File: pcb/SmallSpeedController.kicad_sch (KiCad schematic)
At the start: 38 parts, among them J1 Conn_01x02_Socket, J10 Conn_01x03_Socket, J11 Conn_01x03_Socket, J2 Conn_01x02_Socket, J4 Conn_01x02_Socket, J5 Conn_01x04_Socket, J6 Conn_01x04_Socket, J9 Conn_01x03_Socket, SW2 TS-1088-AR02016, U2 AMS1117-3.3, U3 DRV8837DSGR, U4 DRV8837DSGR, U5 CH32V003FxUx

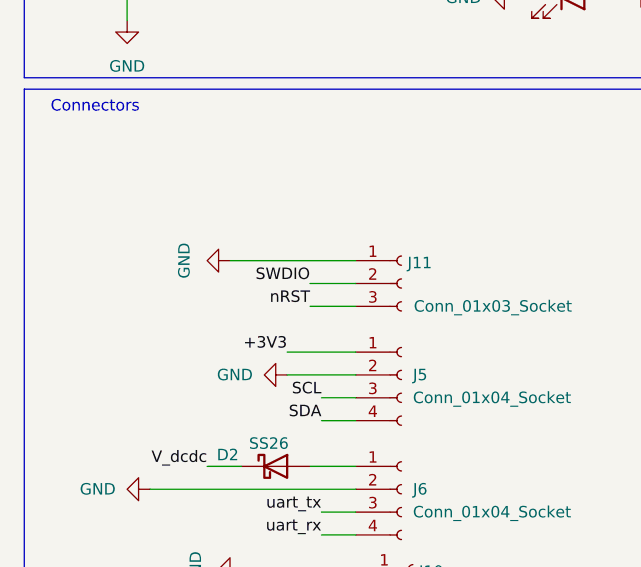
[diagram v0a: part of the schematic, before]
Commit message: pcb, sch: small cleanups for next fabrication round
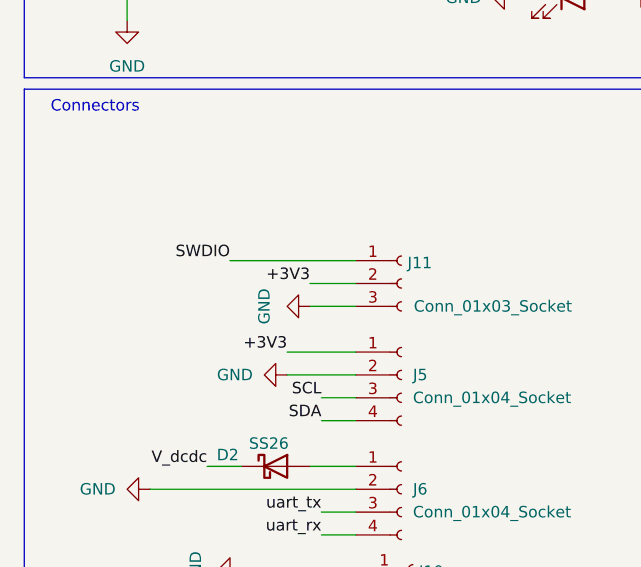
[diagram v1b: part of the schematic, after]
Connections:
- net +3V3: now also J11.2 (Pin_2)
- net GND: now also J11.3 (Pin_3); no longer J11.1 (Pin_1)
- net SWDIO: now also J11.1 (Pin_1); no longer J11.2 (Pin_2)
- net nRST: no longer J11.3 (Pin_3)
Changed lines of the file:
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@@
 		)
 	)
-	(label "SWDIO"
+	(label "+3V3"
 		(at 50.8 148.59 180)
 		(effects
@@
 		)
 	)
-	(label "nRST"
-		(at 50.8 151.13 180)
-		(effects
-			(font
-				(size 1.27 1.27)
-			)
-			(justify right bottom)
-		)
-	)
 	(label "pwm_speed_input2"
 		(at 201.93 170.18 0)
@@
 		)
 	)
+	(label "SWDIO"
+		(at 41.91 146.05 180)
+		(effects
+			(font
+				(size 1.27 1.27)
+			)
+			(justify right bottom)
+		)
+	)
 	(label "motcon1_pwm_in1"
 		(at 181.61 43.18 0)
@@
 	)
 	(symbol
+		(lib_id "power:GND")
+		(at 50.8 151.13 270)
+		(unit 1)
+		(exclude_from_sim no)
+		(in_bom yes)
+		(on_board yes)
+		(dnp no)
+		(property "Reference" "#PWR010"
+			(at 44.45 151.13 0)
+			(effects
+				(font
+					(size 1.27 1.27)
+				)
+				(hide yes)
+			)
+		)
+		(property "Value" "GND"
+			(at 45.72 151.13 0)
+			(effects
+				(font
+					(size 1.27 1.27)
+				)
+			)
+		)
+		(property "Footprint" ""
+			(at 50.8 151.13 0)
+			(effects
+				(font
+					(size 1.27 1.27)
+				)
+				(hide yes)
+			)
+		)
+		(property "Datasheet" ""
+			(at 50.8 151.13 0)
+			(effects
+				(font
+					(size 1.27 1.27)
+				)
+				(hide yes)
+			)
+		)
+		(property "Description" "Power symbol creates a global label with name \"GND\" , ground"
+			(at 50.8 151.13 0)
+			(effects
+				(font
+					(size 1.27 1.27)
+				)
+				(hide yes)
+			)
+		)
+		(pin "1"
+		)
+		(instances
+			(project "SmallSpeedController"
+				(path "/ad61fa74-e1dd-4b78-9d6b-122c1a722d03"
+					(reference "#PWR010")
+					(unit 1)
+				)
+			)
+		)
+	)
+	(symbol
 		(lib_id "Device:C")
 		(at 130.81 91.44 0)
@@
 					(unit 1)
 				)
-			)
-		)
-	)
-	(symbol
-		(lib_id "power:GND")
-		(at 41.91 146.05 270)
-		(unit 1)
-		(exclude_from_sim no)
-		(in_bom yes)
-		(on_board yes)
-		(dnp no)
-		(property "Reference" "#PWR031"
-			(at 35.56 146.05 0)
-			(effects
-				(font
-					(size 1.27 1.27)
-				)
-				(hide yes)
-			)
-		)
-		(property "Value" "GND"
-			(at 36.83 146.05 0)
-			(effects
-				(font
-					(size 1.27 1.27)
-				)
-			)
-		)
-		(property "Footprint" ""
-			(at 41.91 146.05 0)
-			(effects
-				(font
-					(size 1.27 1.27)
-				)
-				(hide yes)
-			)
-		)
-		(property "Datasheet" ""
-			(at 41.91 146.05 0)
-			(effects
-				(font
-					(size 1.27 1.27)
-				)
-				(hide yes)
-			)
-		)
-		(property "Description" "Power symbol creates a global label with name \"GND\" , ground"
-			(at 41.91 146.05 0)
-			(effects
-				(font
-					(size 1.27 1.27)
-				)
-				(hide yes)
-			)
-		)
-		(pin "1"
-		)
-		(instances
-			(project "MiniRiscVBot"
-				(path "/ad61fa74-e1dd-4b78-9d6b-122c1a722d03"
-					(reference "#PWR031")
-					(unit 1)
-				)

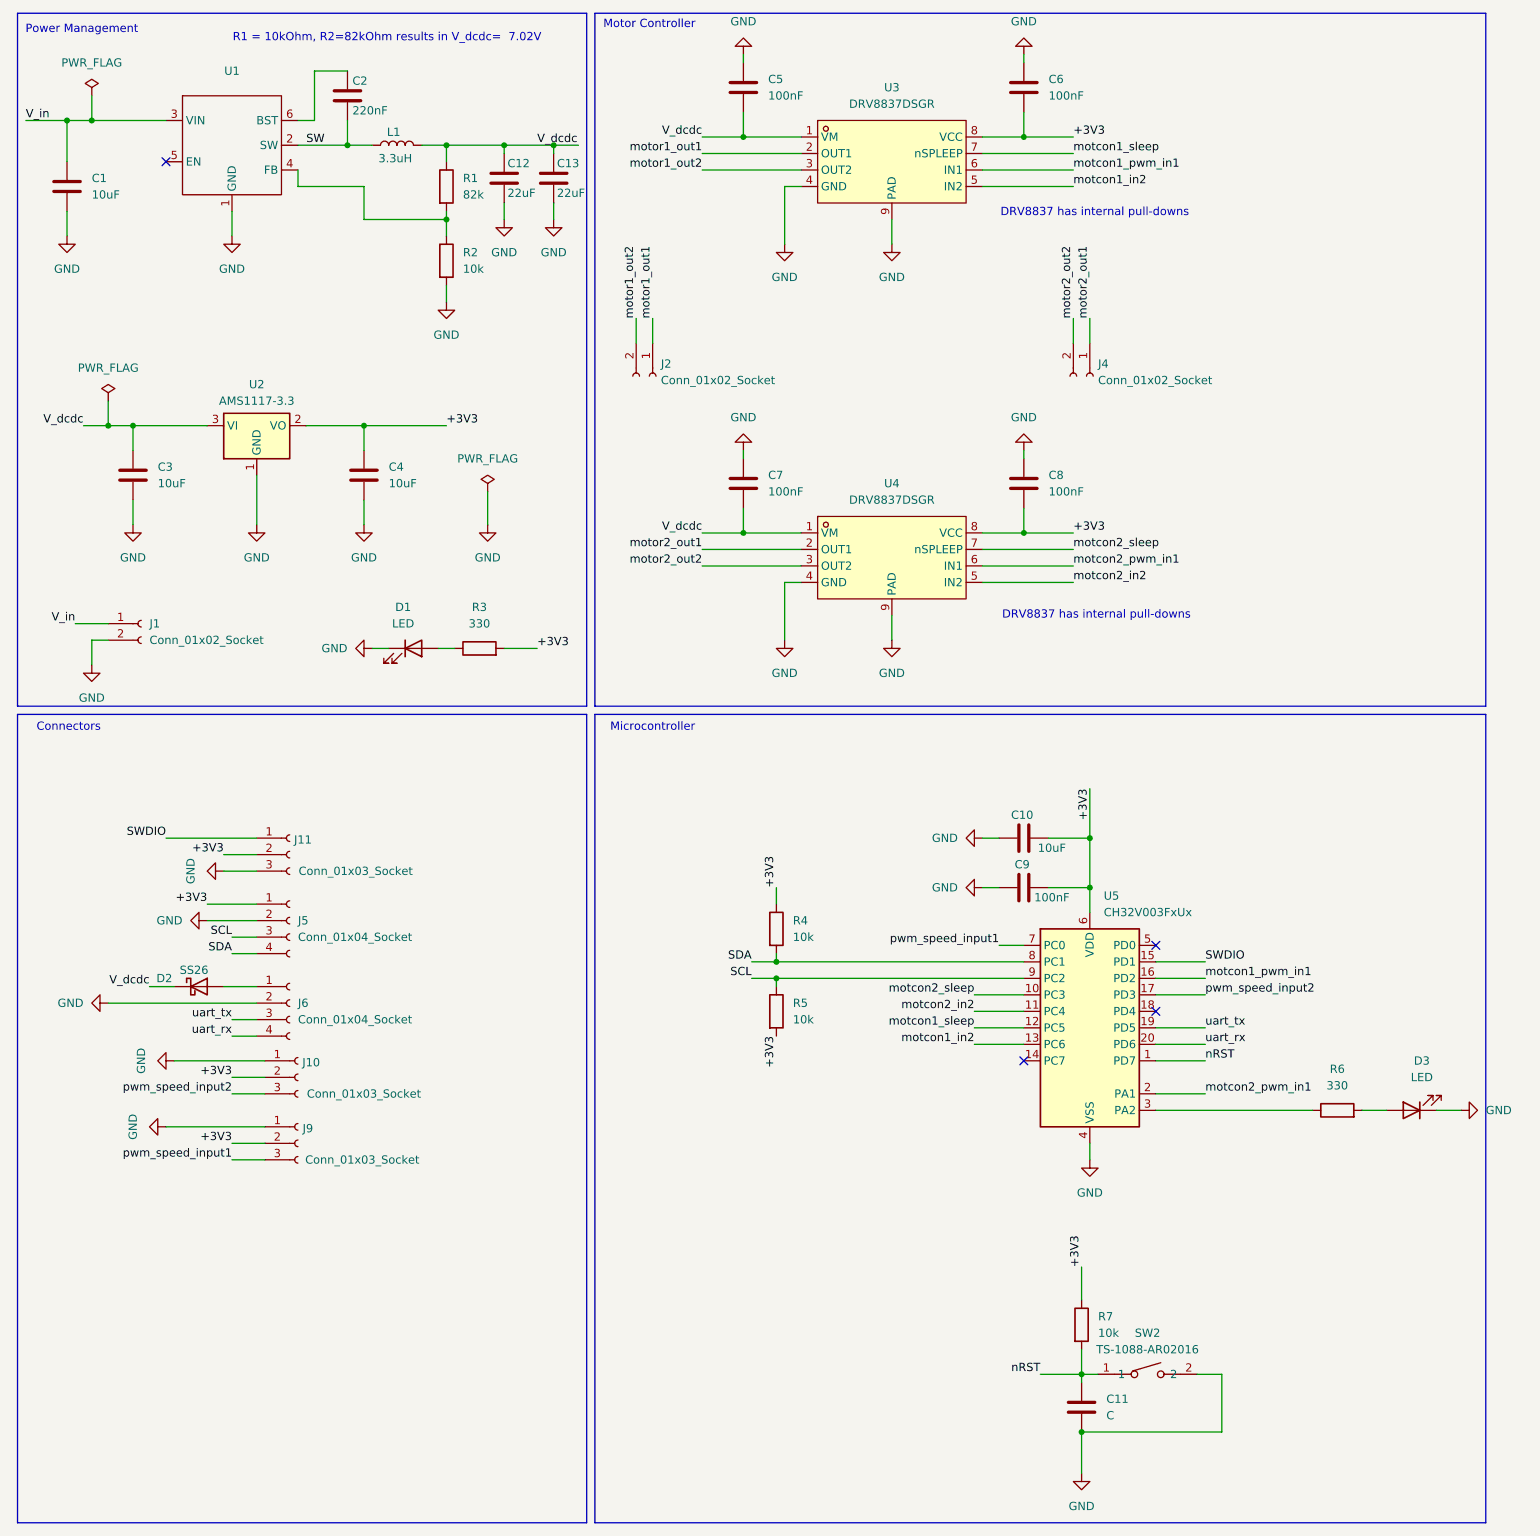
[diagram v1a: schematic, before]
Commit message: pcb: smaller board optimizations, no functional changes
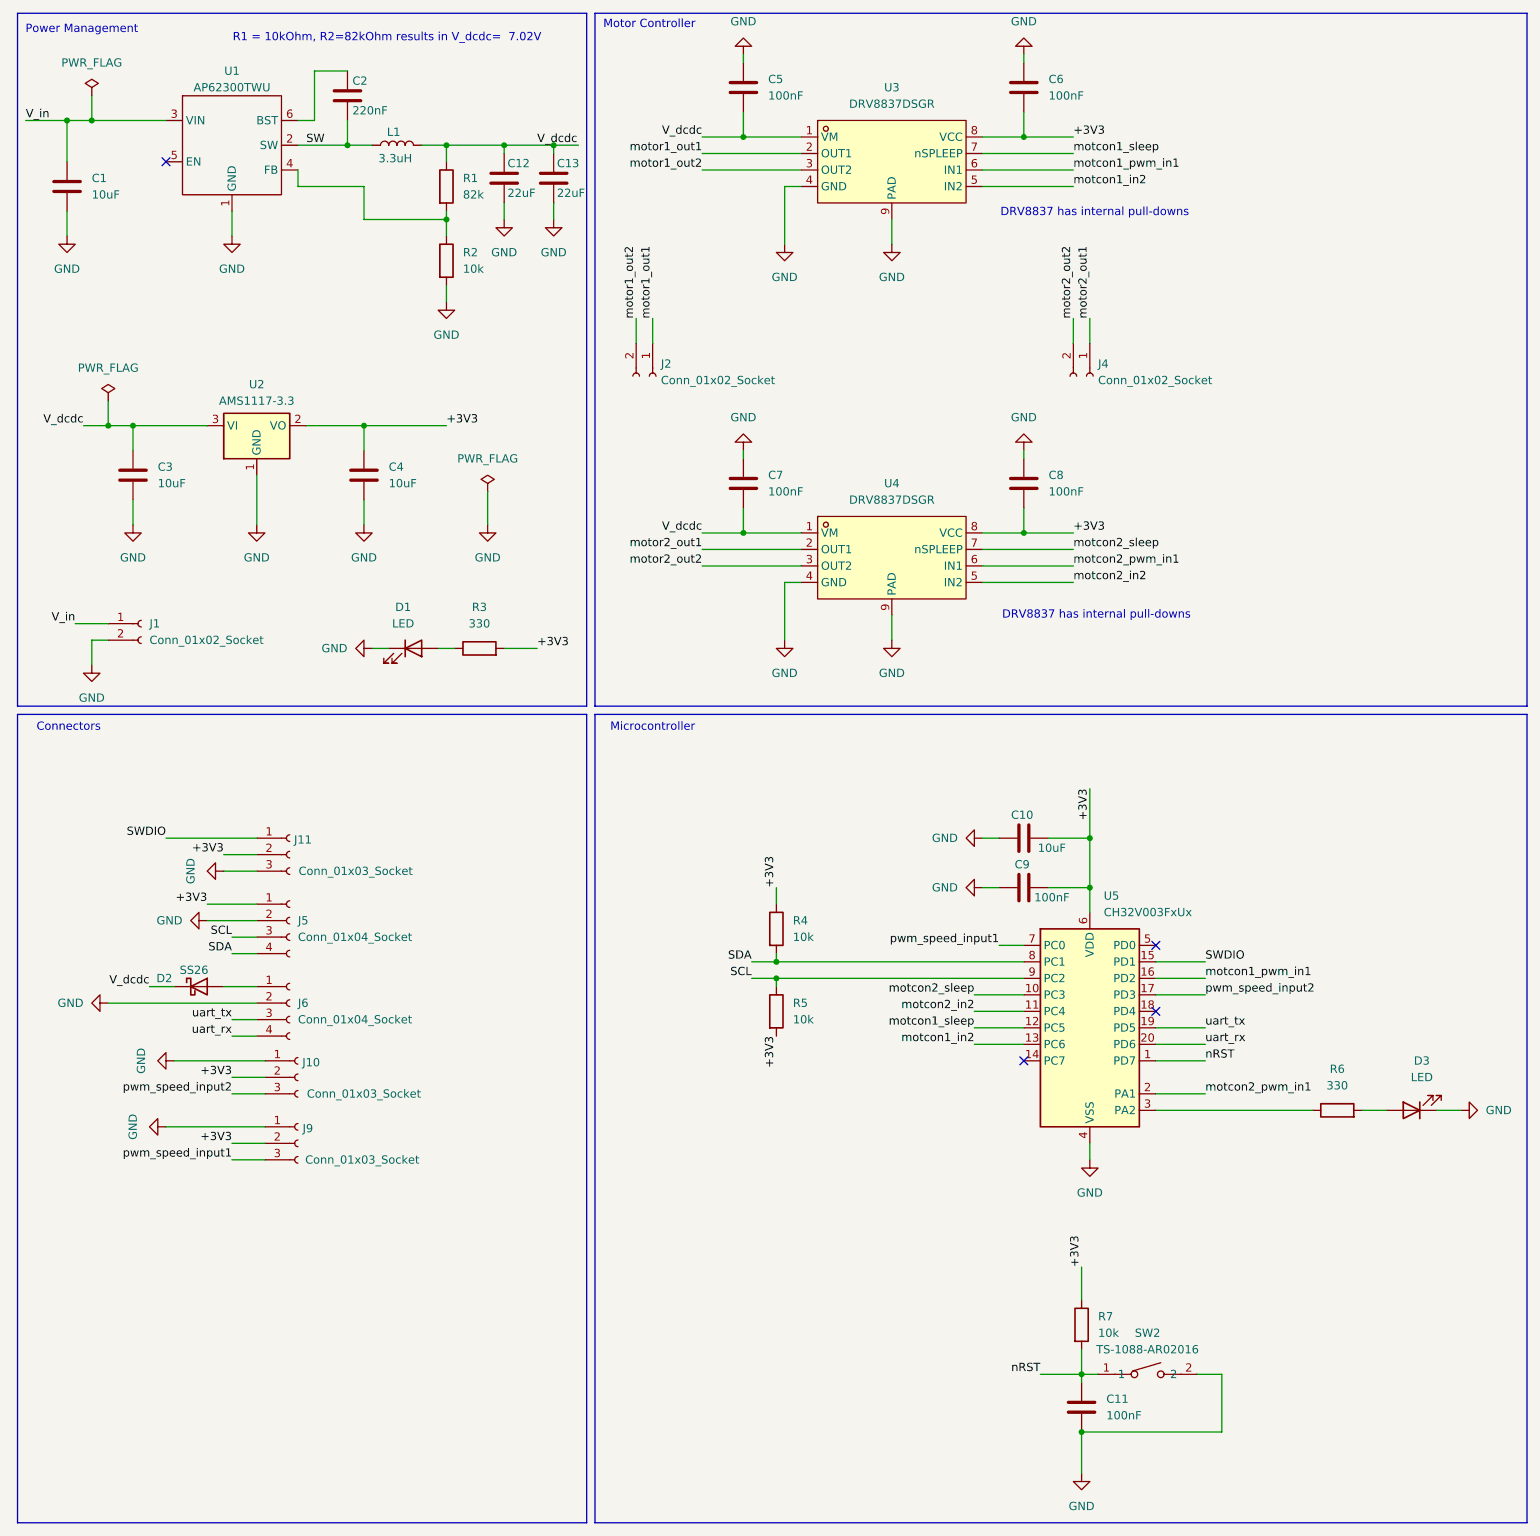
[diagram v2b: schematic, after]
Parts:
- C11: value C -> 100nF
- U1: value ~ -> AP62300TWU
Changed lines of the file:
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@@
 	(rectangle
 		(start 107.95 127)
-		(end 245.11 251.46)
+		(end 251.46 251.46)
 		(stroke
 			(width 0)
@@
 	(rectangle
 		(start 107.95 19.05)
-		(end 245.11 125.73)
+		(end 251.46 125.73)
 		(stroke
 			(width 0)
@@
 			)
 		)
-		(property "Value" "C"
+		(property "Value" "100nF"
 			(at 186.69 234.9499 0)
 			(effects
@@
 			)
 		)
-		(property "Value" "~"
+		(property "Value" "AP62300TWU"
 			(at 52.07 30.48 0)
 			(effects

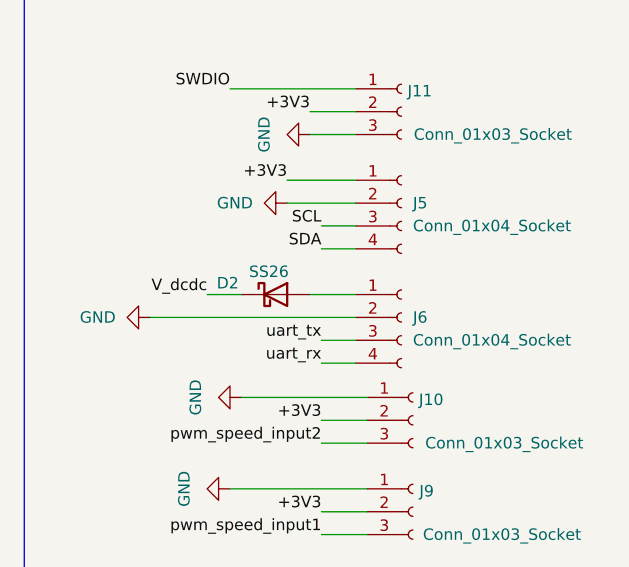
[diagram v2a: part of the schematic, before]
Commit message: pcb: give 3v3 on the UART connector and get rid of diode
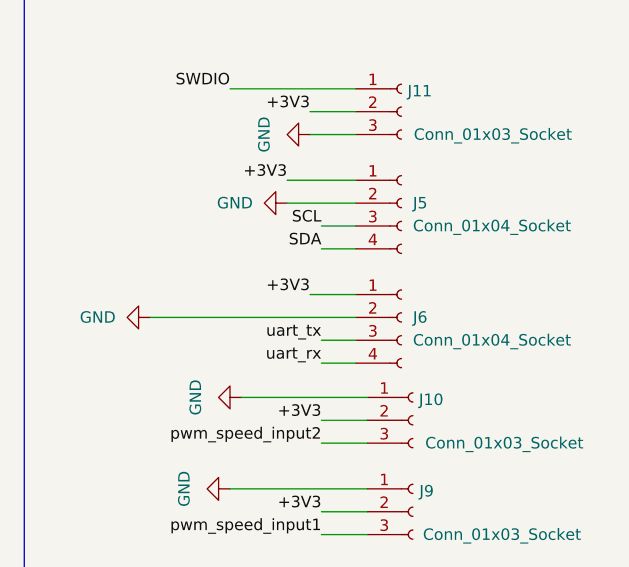
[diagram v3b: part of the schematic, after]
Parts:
- removed D2: SS26, Diode_SMD:D_SMA, symbol Diode:SS26
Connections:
- net +3V3: now also J6.1 (Pin_1)
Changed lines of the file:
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@@
 	(wire
 		(pts
-			(xy 39.37 168.91) (xy 43.18 168.91)
-		)
-		(stroke
-			(width 0)
-			(type default)
-		)
-	)
-	(wire
-		(pts
 			(xy 85.09 49.53) (xy 85.09 50.8)
 		)
@@
 		)
 	)
-	(label "V_dcdc"
-		(at 39.37 168.91 180)
-		(effects
-			(font
-				(size 1.27 1.27)
-			)
-			(justify right bottom)
-		)
-	)
 	(label "uart_rx"
 		(at 201.93 177.8 0)
@@
 		)
 	)
+	(label "+3V3"
+		(at 50.8 168.91 180)
+		(effects
+			(font
+				(size 1.27 1.27)
+			)
+			(justify right bottom)
+		)
+	)
 	(label "motcon2_sleep"
 		(at 181.61 101.6 0)
@@
 					(unit 1)
 				)
-			)
-		)
-	)
-	(symbol
-		(lib_id "Diode:SS26")
-		(at 46.99 168.91 0)
-		(unit 1)
-		(exclude_from_sim no)
-		(in_bom yes)
-		(on_board yes)
-		(dnp no)
-		(property "Reference" "D2"
-			(at 41.656 167.64 0)
-			(effects
-				(font
-					(size 1.27 1.27)
-				)
-			)
-		)
-		(property "Value" "SS26"
-			(at 46.228 166.37 0)
-			(effects
-				(font
-					(size 1.27 1.27)
-				)
-			)
-		)
-		(property "Footprint" "Diode_SMD:D_SMA"
-			(at 46.99 173.355 0)
-			(effects
-				(font
-					(size 1.27 1.27)
-				)
-				(hide yes)
-			)
-		)
-		(property "Datasheet" "https://www.vishay.com/docs/88748/ss22.pdf"
-			(at 46.99 168.91 0)
-			(effects
-				(font
-					(size 1.27 1.27)
-				)
-				(hide yes)
-			)
-		)
-		(property "Description" "60V 2A Schottky Diode, SMA"
-			(at 46.99 168.91 0)
-			(effects
-				(font
-					(size 1.27 1.27)
-				)
-				(hide yes)
-			)
-		)
-		(property "Sim.Device" ""
-			(at 46.99 168.91 0)
-			(effects
-				(font
-					(size 1.27 1.27)
-				)
-			)
-		)
-		(pin "2"
-		)
-		(pin "1"
-		)
-		(instances
-			(project ""
-				(path "/ad61fa74-e1dd-4b78-9d6b-122c1a722d03"
-					(reference "D2")
-					(unit 1)
-				)

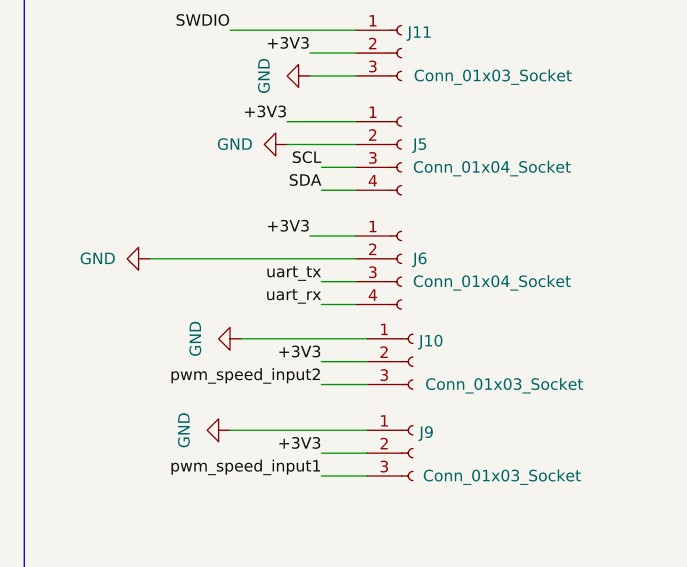
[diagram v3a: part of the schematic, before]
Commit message: pcb: restore symmetry after diode was removed
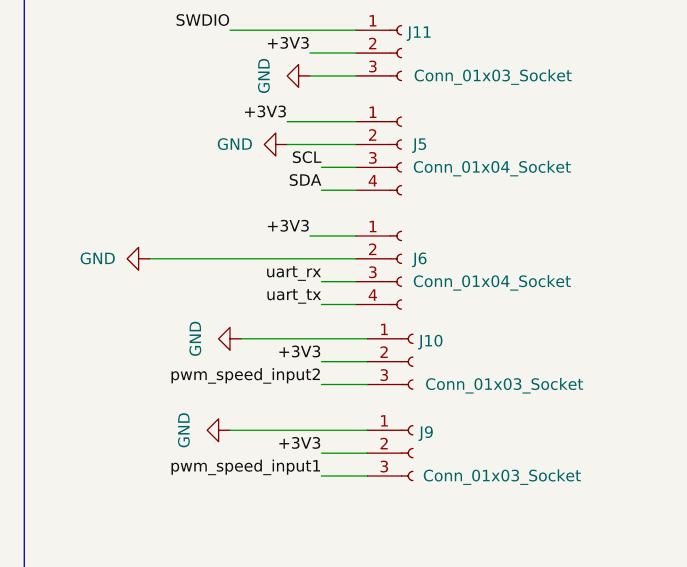
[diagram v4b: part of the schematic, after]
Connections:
- net uart_rx: now also J6.3 (Pin_3); no longer J6.4 (Pin_4)
- net uart_tx: now also J6.4 (Pin_4); no longer J6.3 (Pin_3)
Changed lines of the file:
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@@
+	(wire
+		(pts
+			(xy 52.07 173.99) (xy 55.88 173.99)
+		)
+		(stroke
+			(width 0)
+			(type default)
+		)
+	)
 	(wire
 		(pts
@@
 	(wire
 		(pts
-			(xy 52.07 173.99) (xy 55.88 173.99)
-		)
-		(stroke
-			(width 0)
-			(type default)
-		)
-	)
-	(wire
-		(pts
 			(xy 139.7 106.68) (xy 137.16 106.68)
 		)
@@
 	(wire
 		(pts
+			(xy 52.07 176.53) (xy 55.88 176.53)
+		)
+		(stroke
+			(width 0)
+			(type default)
+		)
+	)
+	(wire
+		(pts
 			(xy 137.16 45.72) (xy 137.16 54.61)
 		)
@@
 		(pts
 			(xy 135.89 167.64) (xy 135.89 168.91)
-		)
-		(stroke
-			(width 0)
-			(type default)
-		)
-	)
-	(wire
-		(pts
-			(xy 52.07 176.53) (xy 55.88 176.53)
 		)
 		(stroke
@@
 	)
 	(label "uart_tx"
+		(at 52.07 176.53 180)
+		(effects
+			(font
+				(size 1.27 1.27)
+			)
+			(justify right bottom)
+		)
+	)
+	(label "uart_rx"
 		(at 52.07 173.99 180)
 		(effects
 			(font
-				(size 1.27 1.27)
-			)
-			(justify right bottom)
-		)
-	)
-	(label "uart_rx"
-		(at 52.07 176.53 180)
-		(effects
-			(font
